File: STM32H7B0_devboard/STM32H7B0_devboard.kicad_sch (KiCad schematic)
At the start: 5 parts, among them SW1 SW_SPDT, U1 STM32H7B0VBT6

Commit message: LSE
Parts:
- added C10: 1u, symbol Device:C_Small
- added C11: 10n, symbol Device:C_Small
- added C12, C13: 12p, symbol Device:C_Small
- added C3: 4u7, symbol Device:C_Small
- added C4, C5, C6, C7, C8, C9: 100n, symbol Device:C_Small
- added L1: 39n, symbol Device:L_Small
- added R2: 47, symbol Device:R_Small
- added Y1: 25MHz, symbol Device:Crystal_GND24
- added Y2: 32.768KHz, symbol Device:Crystal
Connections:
- net +3.3VA: now also C10.1, C11.1, L1.1
- net +3V3: now also C3.1, C4.1, C5.1, C6.1, C7.1, C8.1, C9.1, L1.2
- net GND: now also C10.2, C11.2, C12.2, C13.2, C3.2, C4.2, C5.2, C6.2, C7.2, C8.2, C9.2
- net LSE_IN: now also C13.1, Y2.1
- net LSE_OUT: now also R2.1
- net STATUS_LED: now reaches U1.15 (PC0)
- net SPI2_NSS renamed SPI2_NCS
- new net: C12.1, R2.2, Y2.2
- no-connect marks 0 -> 61
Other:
- note added: "Cload (per cap) = 2 * (Yload - Cstray) (Cstray = 2 ~ 10)"
- note added: "TODO"
- note added: "TODO: CMOS instead of Crystal (more precise and lower power!)"
- note added: "TODO: More filtering? (RNG uses analog)"
- moved on the sheet: C1, C2, U1

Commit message: Schematic V0
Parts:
- added C14, C15: 20p, symbol Device:C_Small
- added C16: 10u, symbol Device:C_Small
- added C17: 100n, symbol Device:C_Small
- added C18, C19: 22u, symbol Device:C_Small
- added D1: Blue, symbol Device:LED_Small
- added D2: B5819W, symbol Device:D_Schottky_Small
- added D3: Red, symbol Device:LED_Small
- added F1: 250mA, symbol Device:Polyfuse_Small
- added FB1: 600ohm @ 600MHz, symbol Device:FerriteBead_Small
- added J1: SWD, symbol Connector_Generic:Conn_02x05_Odd_Even
- added J2: 24LC512 socet, symbol Connector_Generic:Conn_02x04_Counter_Clockwise
- added L2: 2u2, symbol Device:L_Small
- added P1: USB_C, symbol Connector:USB_C_Plug_USB2.0
- added Q1: AO3401A, Package_TO_SOT_SMD:SOT-23, symbol Transistor_FET:AO3401A
- added R10, R11, R12, R15, R16, R19, R20, R9: 22, symbol Device:R_Small
- added R13, R14: 2k2, symbol Device:R_Small
- added R17, R18: 5k1, symbol Device:R_Small
- added R21: 1k, symbol Device:R_Small
- added R3: 47, symbol Device:R_Small
- added R4: 1k5, symbol Device:R_Small
- added R5: 100k, symbol Device:R_Small
- added R6: 68k, symbol Device:R_Small
- added R7: 33k2, symbol Device:R_Small
- added R8: 10k, symbol Device:R_Small
- added U2: ~, symbol Marijn:TPS563201DDCR
- added U3: USBLC6-2SC6, Package_TO_SOT_SMD:SOT-23-6, symbol Power_Protection:USBLC6-2SC6
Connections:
- net +3V3: now also C18.1, C19.1, D3.2 (A), J1.1 (Pin_1), J2.8 (Pin_8), L2.2, R13.1, R14.1, R7.1
- net GND: now also Y1.2, Y1.4, C14.2, C15.2, C16.2, C18.2, C19.2, J1.3 (Pin_3), J1.5 (Pin_5), J1.9 (Pin_9), J2.1 (Pin_1), J2.2 (Pin_2), J2.3 (Pin_3), J2.4 (Pin_4), J2.7 (Pin_7), P1.A1 (GND), P1.A12 (GND), P1.B1 (GND), P1.B12 (GND), P1.S1 (SHIELD), Q1.1 (G), R17.2, R18.2, R21.2, R4.1, R6.1, R8.1, U2.1 (GND), U3.2 (GND)
- net HSE_IN: now also Y1.1, C14.1
- net HSE_OUT: now also R3.1
- net I2C_SCL: now also R13.2, R15.1
- net I2C_SDA: now also R14.2, R16.1
- net NRST: now also R12.2
- net STATUS_LED: now also D1.2 (A)
- net SWCLK: now also R10.2
- net SWDIO: now also R9.2
- net SWO: now also R11.2
- net USB_DM: now also U3.3 (I/O2)
- net USB_DP: now also U3.1 (I/O1)
- net at Y1.3: now also C15.1, R3.2
- new net: P1.A6 (D+), R20.1
- new net: P1.A7 (D-), R19.1
- new net: D2.1 (K), FB1.1, Q1.2 (S)
- new net: D3.1 (K), R21.1
- new net: F1.2, Q1.3 (D)
- new net: J2.5 (Pin_5), R16.2
- new net: J2.6 (Pin_6), R15.2
- new net: D1.1 (K), R4.2
- new net +12V: F1.1
- new net +5V: D2.2 (A), P1.A4 (VBUS), P1.A9 (VBUS), P1.B4 (VBUS), P1.B9 (VBUS), U3.5 (VBUS)
- new net BUCK_BST: C17.2, U2.6 (VBST)
- new net BUCK_EN: R5.1, R6.2, U2.5 (EN)
- new net BUCK_FB: R7.2, R8.2, U2.4 (VFB)
- new net BUCK_IN: C16.1, FB1.2, R5.2, U2.3 (VIN)
- new net BUCK_SW: C17.1, L2.1, U2.2 (SW)
- new net CC1: P1.A5 (CC), R17.1
- new net CC2: P1.B5 (VCONN), R18.1
- new net NRST_CONN: J1.10 (Pin_10), R12.1
- new net SWCLK_CONN: J1.4 (Pin_4), R10.1
- new net SWDIO_CONN: J1.2 (Pin_2), R9.1
- new net SWO_CONN: J1.6 (Pin_6), R11.1
- new net USB_CONN_DM: R19.2, U3.4 (I/O2)
- new net USB_CONN_DP: R20.2, U3.6 (I/O1)
- no-connect marks 61 -> 63
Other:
- note added: "3V3"
- note added: "3V3 Analog"
- note added: "BUCK"
- note added: "Ferrite Bead?"
- note added: "I2C"
- note added: "LED"
- note added: "LSE / HSE"
- note added: "P-channel for polarity protection?"
- note added: "STM32H7B0vbt6"
- note added: "SWD"
- note added: "TODO: determine the maximum current"
- note added: "TODO: solder break!"
- note added: "USB"
- note added: "What does this do?"
- note removed: "TODO"
- moved on the sheet: C1, C10, C11, C12, C13, C2, C3, C4, C5, C6, C7, C8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

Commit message: Schematic V0.1
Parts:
- added J3: FPC socket, symbol Connector:Conn_01x30_Socket
- added R22, R23, R24: 2k2, symbol Device:R_Small
- added R25, R26, R27, R28, R29, R30, R31, R32: 22, symbol Device:R_Small
- added R33: 51, symbol Device:R_Small
- added U4: ~, symbol Marijn:M95P32
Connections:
- net +3V3: now also R22.2, R23.2, R24.2, R25.2, R26.2, R27.2, R33.1, U4.8 (VCC)
- net GND: now also J3.1 (Pin_1), J3.22 (Pin_22), J3.25 (Pin_25), J3.30 (Pin_30), J3.9 (Pin_9), U4.4 (VSS)
- net I2C_SCL: now also R15.2; no longer R15.1
- net I2C_SDA: now also R16.2; no longer R16.1
- net QSPI1_IO0: now also U4.5 (D-DQ0)
- net QSPI1_IO1: now also U4.2 (Q-DQ1)
- net QSPI1_IO2: now also U4.3 (NW-DQ2)
- net QSPI1_IO3: now also U4.7 (NH_DQ3)
- net QSPI1_NCS: now also R22.1, U4.1 (NCS)
- net QSPI1_SCK: now also U4.6 (CLK)
- net SCREEN_cmd_pin: now also R31.2
- net SPI2_MOSI: now also R32.2
- net SPI2_NCS: now also R24.1, R29.2
- net SPI2_SCK: now also R30.2
- net SDA_CONN: now reaches J2.5 (Pin_5)
- net SDA_CONN: now also R16.1; no longer R16.2
- net SCL_CONN: now reaches J2.6 (Pin_6)
- net SCL_CONN: now also R15.1; no longer R15.2
- net LCD_RESET: now reaches U1.47 (PB11)
- net LCD_RESET: now also R23.1, R28.2
- new net FPC_CONN_CS: J3.6 (Pin_6), R29.1
- new net FPC_CONN_IM1: J3.4 (Pin_4), R26.1
- new net FPC_CONN_IM2: J3.3 (Pin_3), R27.1
- new net FPC_CONN_LEDA: J3.20 (Pin_20), R33.2
- new net FPC_CONN_MOSI: J3.10 (Pin_10), R32.1
- new net FPC_CONN_RESET: J3.5 (Pin_5), R28.1
- new net FPC_CONN_RS: J3.8 (Pin_8), R31.1
- new net FPC_CONN_SCK: J3.7 (Pin_7), R30.1
- new net FPC_CONN_VDD: J3.2 (Pin_2), R25.1
- no-connect marks 63 -> 78
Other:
- note added: "D0-D7"
- note added: "LCD"
- note added: "M95P32"
- note added: "TODO: Check the LEDA volatge MAX: 3v2"
- moved on the sheet: J1, J2, R10, R11, R12, R13, R14, R15, R16, R17, R18, R9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

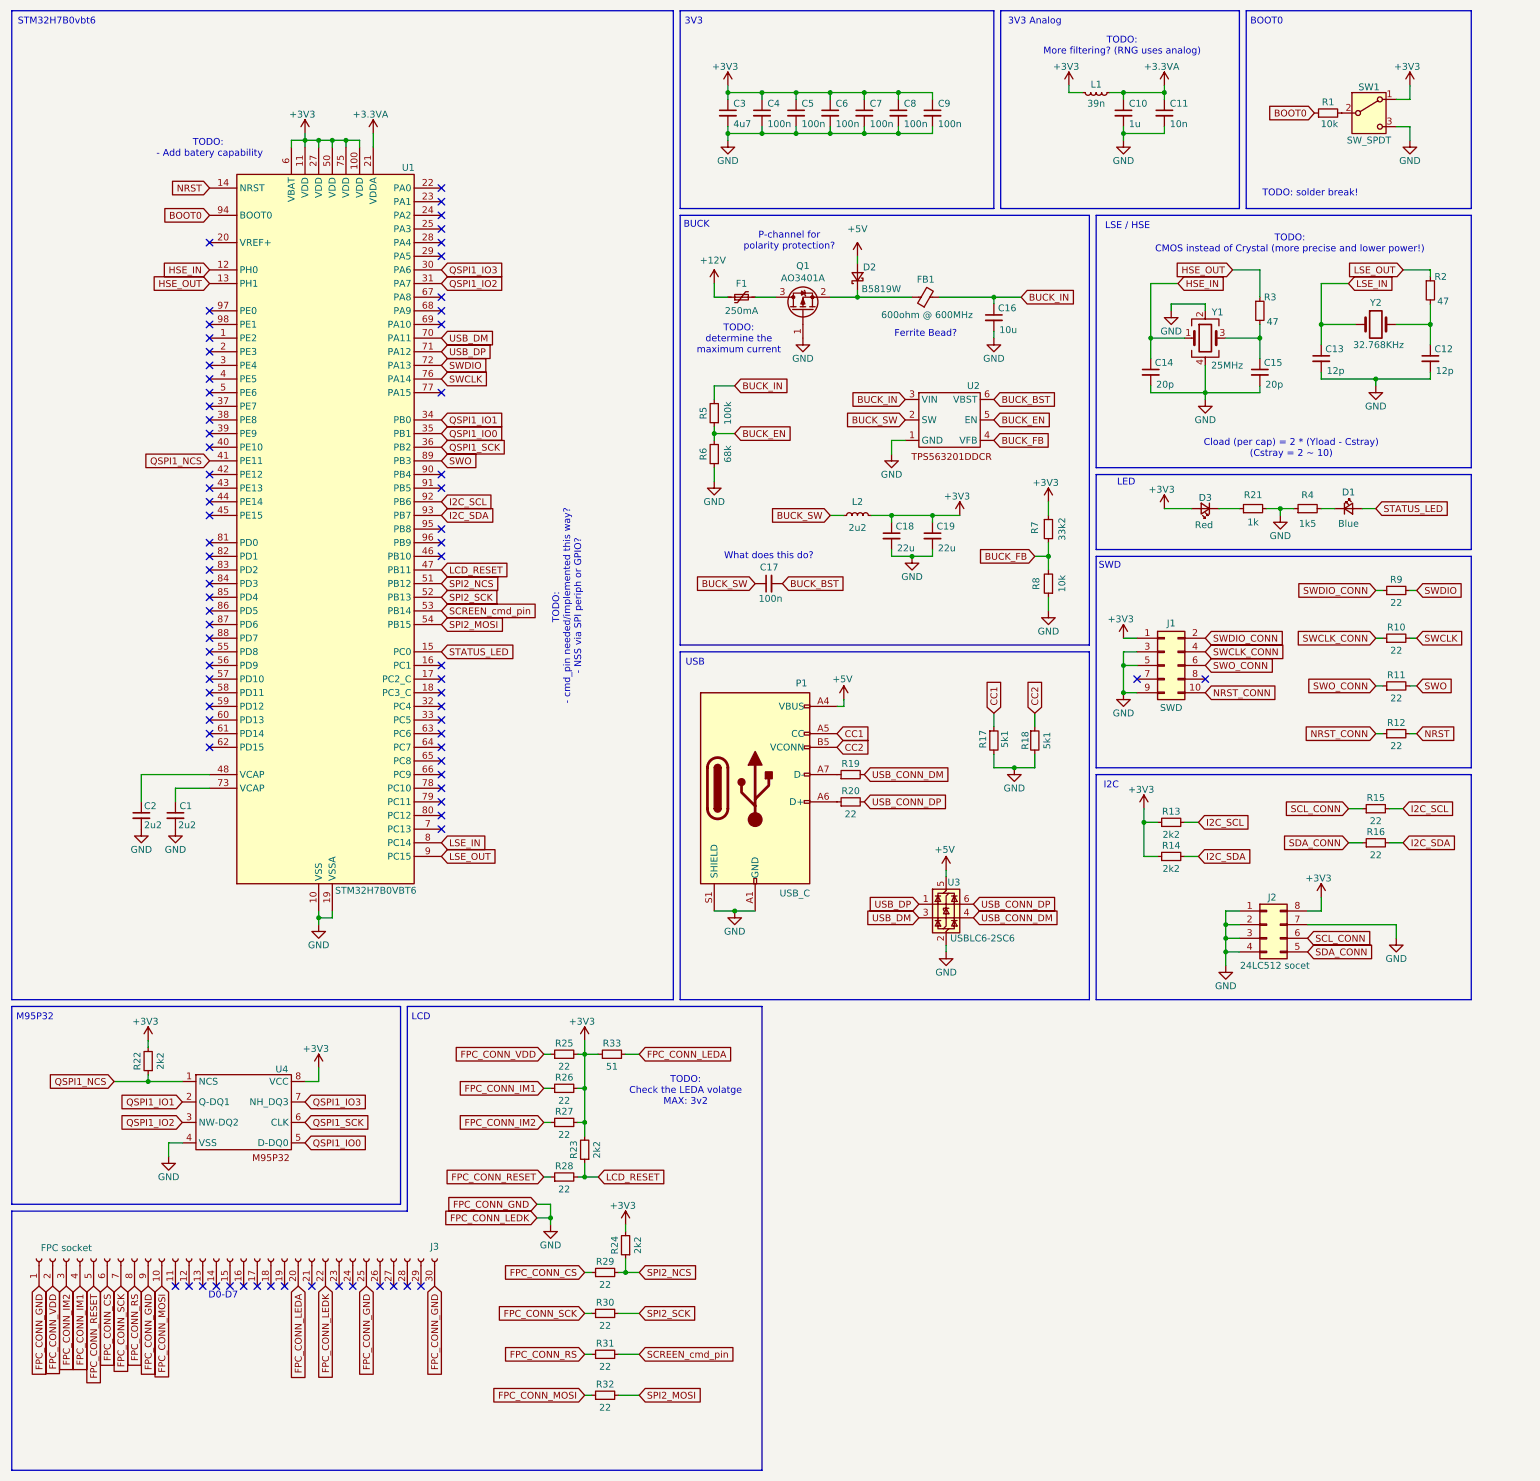
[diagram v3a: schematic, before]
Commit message: Schematic V0.2
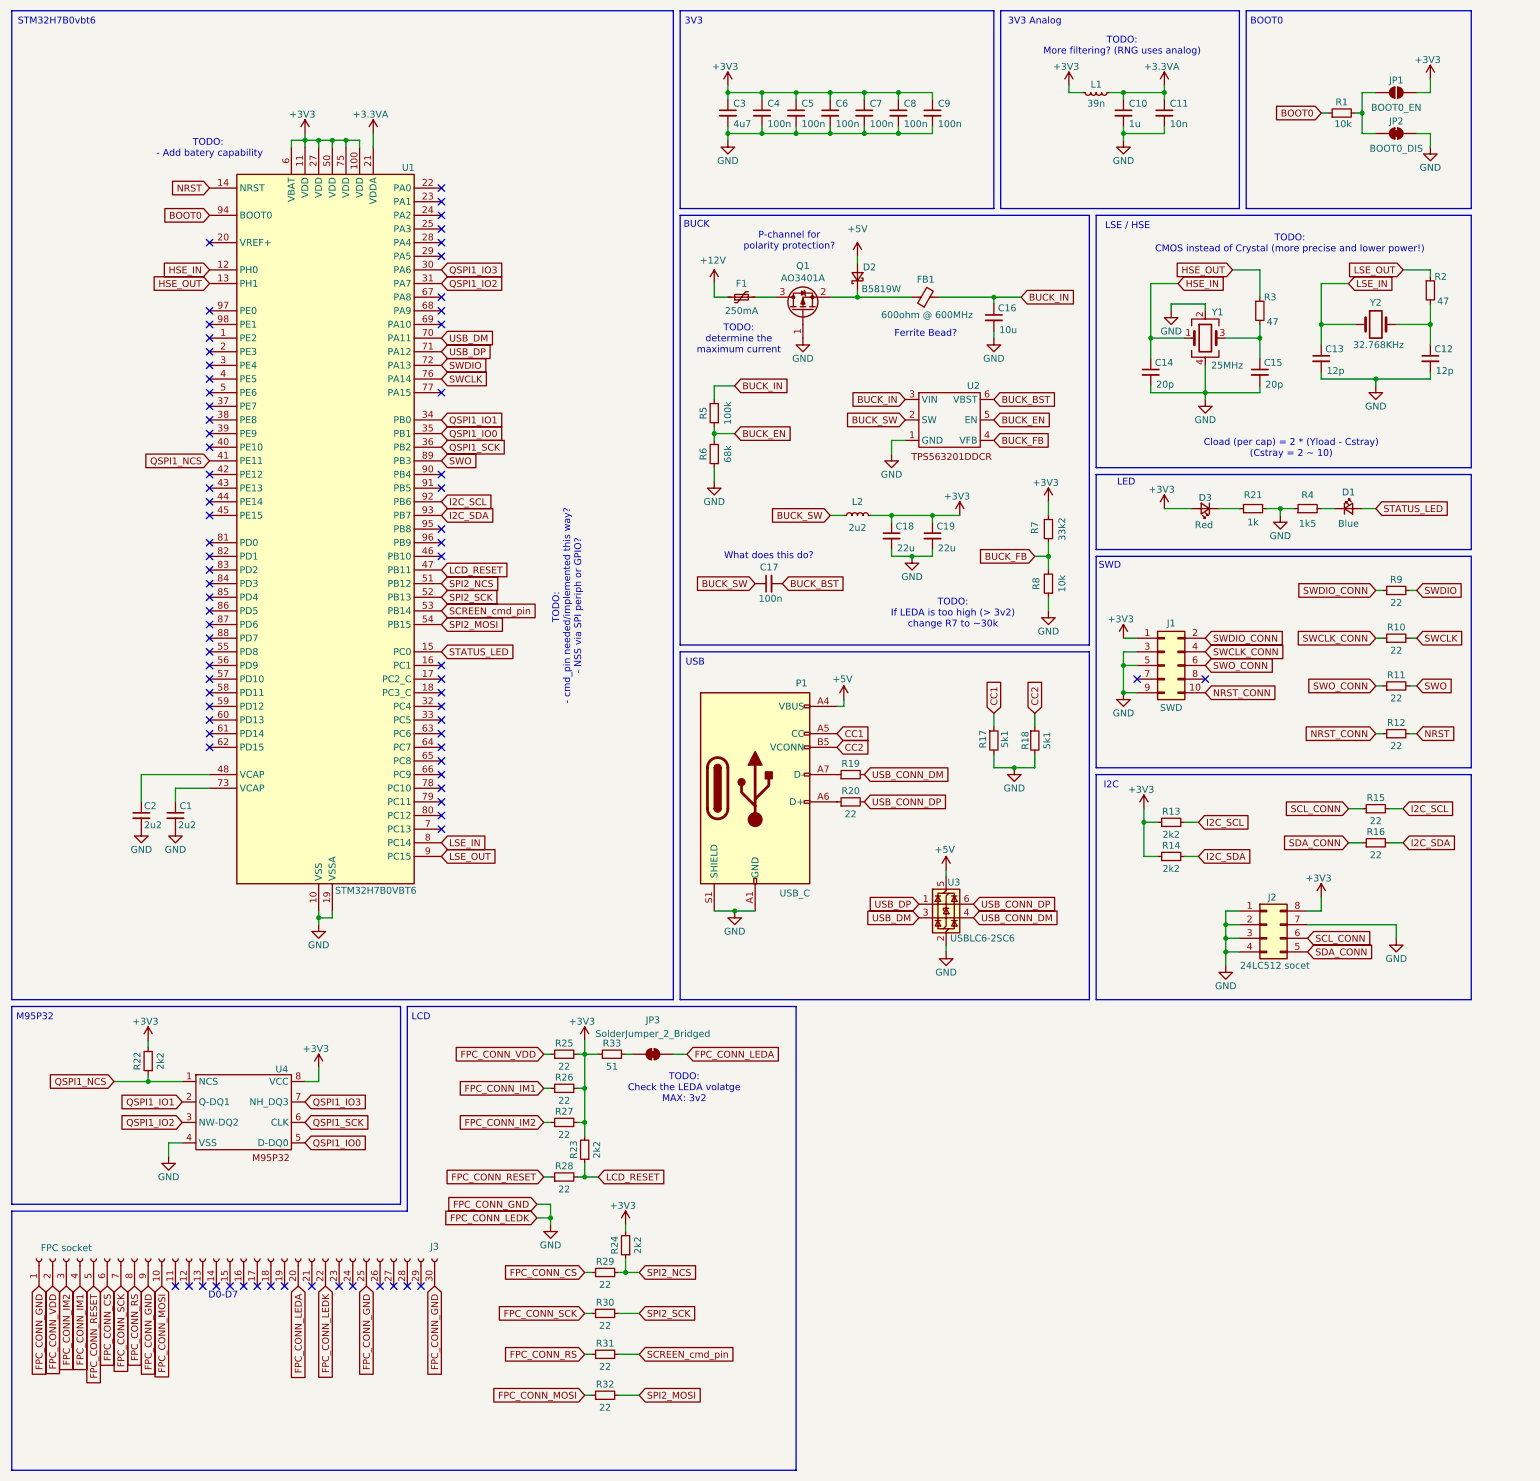
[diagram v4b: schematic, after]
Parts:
- removed SW1: SW_SPDT, symbol Switch:SW_SPDT
- added JP1: BOOT0_EN, symbol Jumper:SolderJumper_2_Open
- added JP2: BOOT0_DIS, symbol Jumper:SolderJumper_2_Bridged
- added JP3: SolderJumper_2_Bridged, symbol Jumper:SolderJumper_2_Bridged
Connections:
- net +3V3: now also JP1.2 (B)
- net FPC_CONN_LEDA: now also JP3.2 (B); no longer R33.2
- net GND: now also JP2.2 (B)
- net at R1.2: now also JP1.1 (A), JP2.1 (A)
- new net: JP3.1 (A), R33.2
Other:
- note added: "TODO: If LEDA is too high (> 3v2) change R7 to ~30k"
- note removed: "TODO: solder break!"
- moved on the sheet: R1

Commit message: Added TODOs
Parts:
- added H1, H2, H3, H4: Mount, MountingHole:MountingHole_4.3mm_M4_Pad_Via, symbol Mechanical:MountingHole_Pad
- C1, C10, C11, C12, C13, C14, C15, C2, C3, C4, C5, C6, C7, C8, C9: footprint (none) -> Capacitor_SMD:C_0402_1005Metric
- C16, C18, C19: footprint (none) -> Capacitor_SMD:C_1206_3216Metric
- C17: footprint (none) -> Capacitor_SMD:C_0603_1608Metric
- D1, D3: footprint (none) -> Diode_SMD:D_0603_1608Metric
- D2: footprint (none) -> Diode_SMD:D_SOD-123
- F1: footprint (none) -> Fuse:Fuse_1206_3216Metric
- FB1: footprint (none) -> Inductor_SMD:L_0805_2012Metric
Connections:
- net GND: now also H1.1, H2.1, H3.1, H4.1
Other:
- note added: "Mount"
- note added: "TODO: Breakout??"
- note added: "TODO: Check the LEDA volatge MAX: 3v2 DAC and opamp buffer (default 0V)"
- note added: "TODO: USB common mode chocke FL2 (O805USB-902ML)"
- note added: "TODO: oscilator instead of Crystal (more precise and lower power!)"
- note removed: "TODO: CMOS instead of Crystal (more precise and lower power!)"
- note removed: "TODO: Check the LEDA volatge MAX: 3v2"

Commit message: Schematic V1.0
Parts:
- removed C16: 10u, Capacitor_SMD:C_1206_3216Metric, symbol Device:C_Small
- removed C17: 100n, Capacitor_SMD:C_0603_1608Metric, symbol Device:C_Small
- removed C18, C19: 22u, Capacitor_SMD:C_1206_3216Metric, symbol Device:C_Small
- removed D2: B5819W, Diode_SMD:D_SOD-123, symbol Device:D_Schottky_Small
- removed F1: 250mA, Fuse:Fuse_1206_3216Metric, symbol Device:Polyfuse_Small
- removed FB1: 600ohm @ 600MHz, Inductor_SMD:L_0805_2012Metric, symbol Device:FerriteBead_Small
- removed J3: FPC socket, symbol Connector:Conn_01x30_Socket
- removed JP1: BOOT0_EN, symbol Jumper:SolderJumper_2_Open
- removed JP2: BOOT0_DIS, symbol Jumper:SolderJumper_2_Bridged
- removed JP3: SolderJumper_2_Bridged, symbol Jumper:SolderJumper_2_Bridged
- removed L2: 2u2, symbol Device:L_Small
- removed P1: USB_C, symbol Connector:USB_C_Plug_USB2.0
- removed Q1: AO3401A, Package_TO_SOT_SMD:SOT-23, symbol Transistor_FET:AO3401A
- removed R1, R8: 10k, symbol Device:R_Small
- removed R17, R18: 5k1, symbol Device:R_Small
- removed R19, R20: 22, symbol Device:R_Small
- removed R33: 51, symbol Device:R_Small
- removed R5: 100k, symbol Device:R_Small
- removed R6: 68k, symbol Device:R_Small
- removed R7: 33k2, symbol Device:R_Small
- removed U2: ~, symbol Marijn:TPS563201DDCR
- removed U3: USBLC6-2SC6, Package_TO_SOT_SMD:SOT-23-6, symbol Power_Protection:USBLC6-2SC6
- added C20: 4u7, Capacitor_SMD:C_1206_3216Metric, symbol Device:C_Small
- added C21: 100n, Capacitor_SMD:C_1206_3216Metric, symbol Device:C_Small
- added Q2: S8050, Package_TO_SOT_SMD:SOT-23, symbol Transistor_BJT:S8050
- added SW1: BOOT_SEL, Button_Switch_SMD:Nidec_Copal_CAS-120A, symbol Switch:SW_Nidec_CAS-120A1
- added U5: ~, symbol Marijn:1.9{dblquote} LCD_FPC_CONN
- R25: value 22 -> 8r2
- R26: value 22 -> 10k
- R27: value 22 -> 1k
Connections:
- net FPC_CONN_IM2 is gone; now on net SCREEN_back_light: R27.1
- net +3V3: now also C20.1, C21.1, SW1.3 (A), U5.2 (VCI), U5.20 (LEDA), U5.3 (IM2), U5.4 (IM1); no longer R25.2, R27.2
- net BOOT0: now also SW1.2 (B)
- net FPC_CONN_CS: now also U5.6 (CS)
- net FPC_CONN_MOSI: now also R32.2, U5.10 (SDA); no longer R32.1
- net FPC_CONN_RESET: now also R28.2, U5.5 (RES); no longer R28.1
- net FPC_CONN_RS: now also R31.2, U5.8 (DC); no longer R31.1
- net FPC_CONN_SCK: now also R30.2, U5.7 (SCL); no longer R30.1
- net GND: now also C20.2, C21.2, Q2.1 (E), SW1.1 (C), U5.1 (GND), U5.11 (DB0), U5.12 (DB1), U5.13 (DB2), U5.14 (DB3), U5.15 (DB4), U5.16 (DB5), U5.17 (DB6), U5.18 (DB7), U5.25 (GND), U5.30 (GND), U5.9 (RD)
- net LCD_RESET: now also R28.1; no longer R28.2
- net SPI2_MOSI: now also R32.1; no longer R32.2
- net SPI2_SCK: now also R30.1; no longer R30.2
- net SCREEN_back_light: now reaches U1.46 (PB10)
- net FPC_CONN_IM1: no longer names the net of R26.1
- net FPC_CONN_IM1: now also R27.2, Q2.2 (B)
- net FPC_CONN_VDD: no longer names the net of R25.1
- net FPC_CONN_VDD: now also Q2.3 (C)
- net SCREEN_cmd_pin renamed SCREEN_cmd
- net SCREEN_cmd: now also R31.1; no longer R31.2
- new net FPC_CONN_LEDK: R25.2, U5.21 (LEDK), U5.22 (LEDK), U5.23 (LEDK), U5.24 (LEDK)
- no-connect marks 78 -> 66
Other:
- added sheet USB (USB.kicad_sch)
- added sheet power (power.kicad_sch)
- note added: "TODO low ESR!!"
- note added: "TODO: remove global labels?"
- note removed: "BUCK"
- note removed: "D0-D7"
- note removed: "Ferrite Bead?"
- note removed: "P-channel for polarity protection?"
- note removed: "TODO: Breakout??"
- note removed: "TODO: Check the LEDA volatge MAX: 3v2 DAC and opamp buffer (default 0V)"
- note removed: "TODO: If LEDA is too high (> 3v2) change R7 to ~30k"
- note removed: "TODO: USB common mode chocke FL2 (O805USB-902ML)"
- note removed: "TODO: determine the maximum current"
- note removed: "USB"
- note removed: "What does this do?"
- moved on the sheet: C10, C11, C12, C13, C14, C15, C3, C4, C5, C6, C7, C8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
